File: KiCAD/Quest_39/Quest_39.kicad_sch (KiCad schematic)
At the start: 15 parts

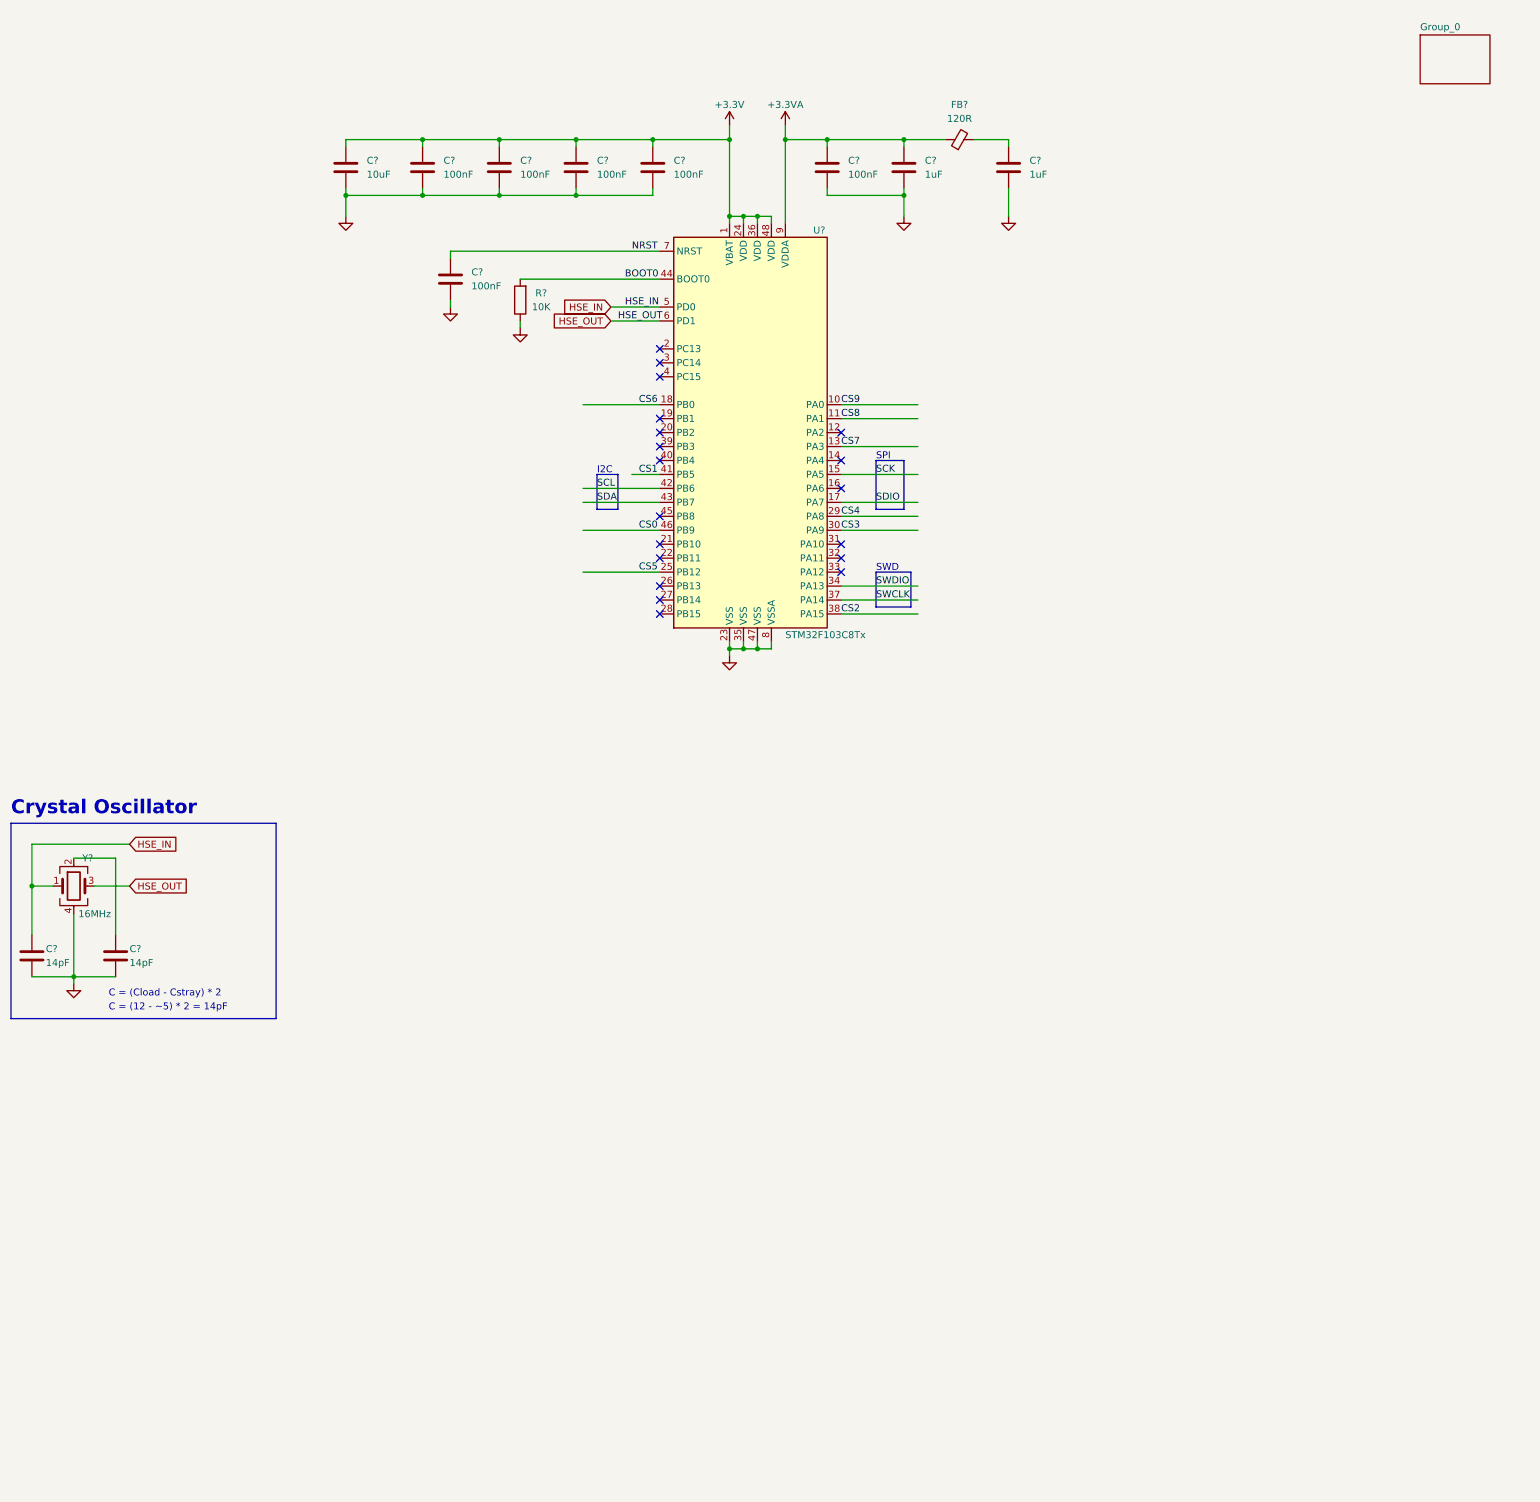
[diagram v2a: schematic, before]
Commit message: Ordered BUCK_x schematic pages
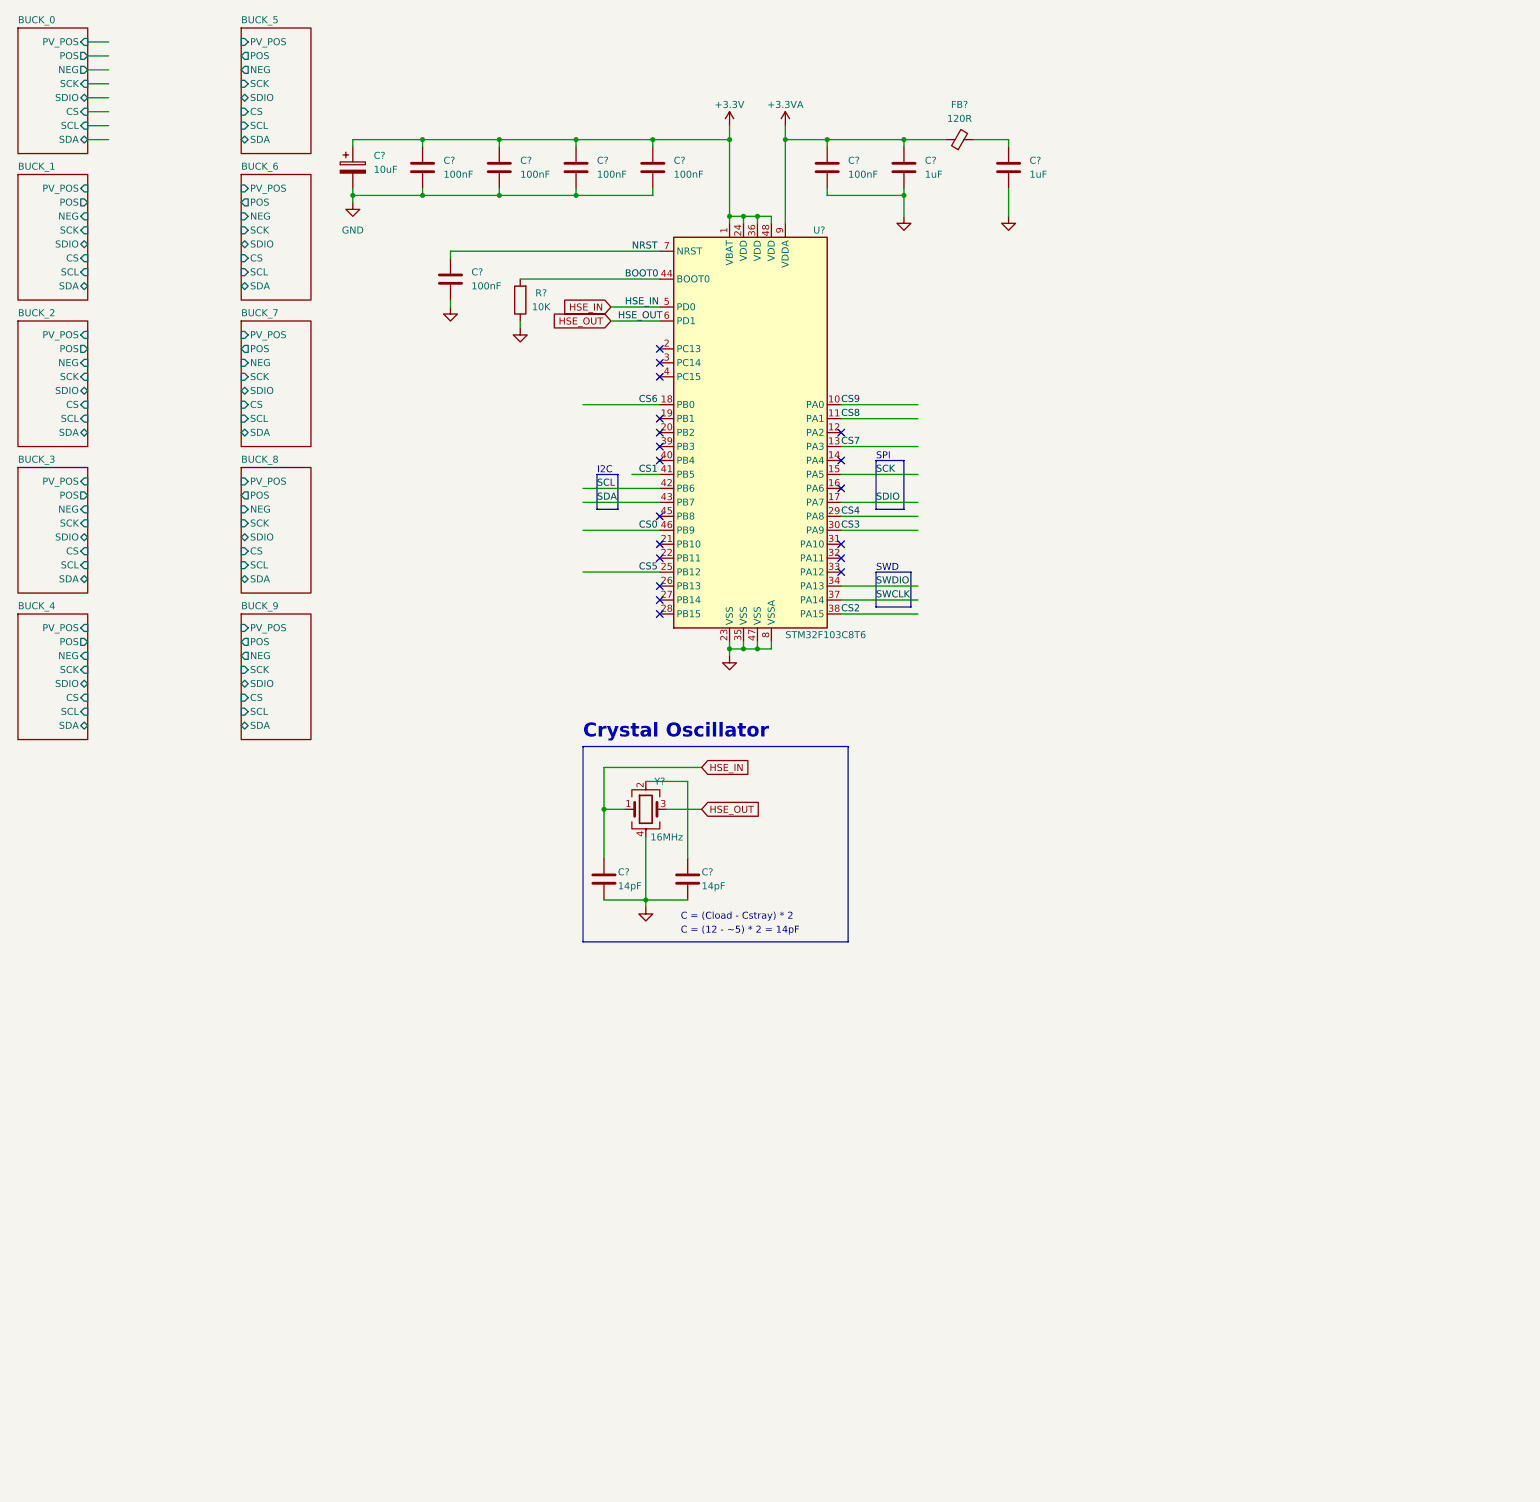
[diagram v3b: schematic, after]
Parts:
- removed C?: 10uF, symbol Device:C
- added C?: 10uF, symbol Device:C_Polarized
- U?: value STM32F103C8Tx -> STM32F103C8T6
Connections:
- net +3.3V: now also C?.1
- net GND: now also C?.2
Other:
- sheet Group_0 renamed BUCK_0
- added sheet BUCK_1 (BUCK_1.kicad_sch)
- added sheet BUCK_2 (BUCK_2.kicad_sch)
- added sheet BUCK_3 (BUCK_3.kicad_sch)
- added sheet BUCK_4 (BUCK_4.kicad_sch)
- added sheet BUCK_5 (BUCK_5.kicad_sch)
- added sheet BUCK_6 (BUCK_6.kicad_sch)
- added sheet BUCK_7 (BUCK_7.kicad_sch)
- added sheet BUCK_8 (BUCK_8.kicad_sch)
- added sheet BUCK_9 (BUCK_9.kicad_sch)
- sheet BUCK_0: file Quest_39_blz2.kicad_sch -> BUCK_0.kicad_sch
- sheet BUCK_0 ports: added CS, NEG, POS, PV_POS, SCK, SCL, SDA, SDIO; removed none
- moved on the sheet: C?, Y?

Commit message: Added screw terminals. Ordered nets and added seperation between systems.
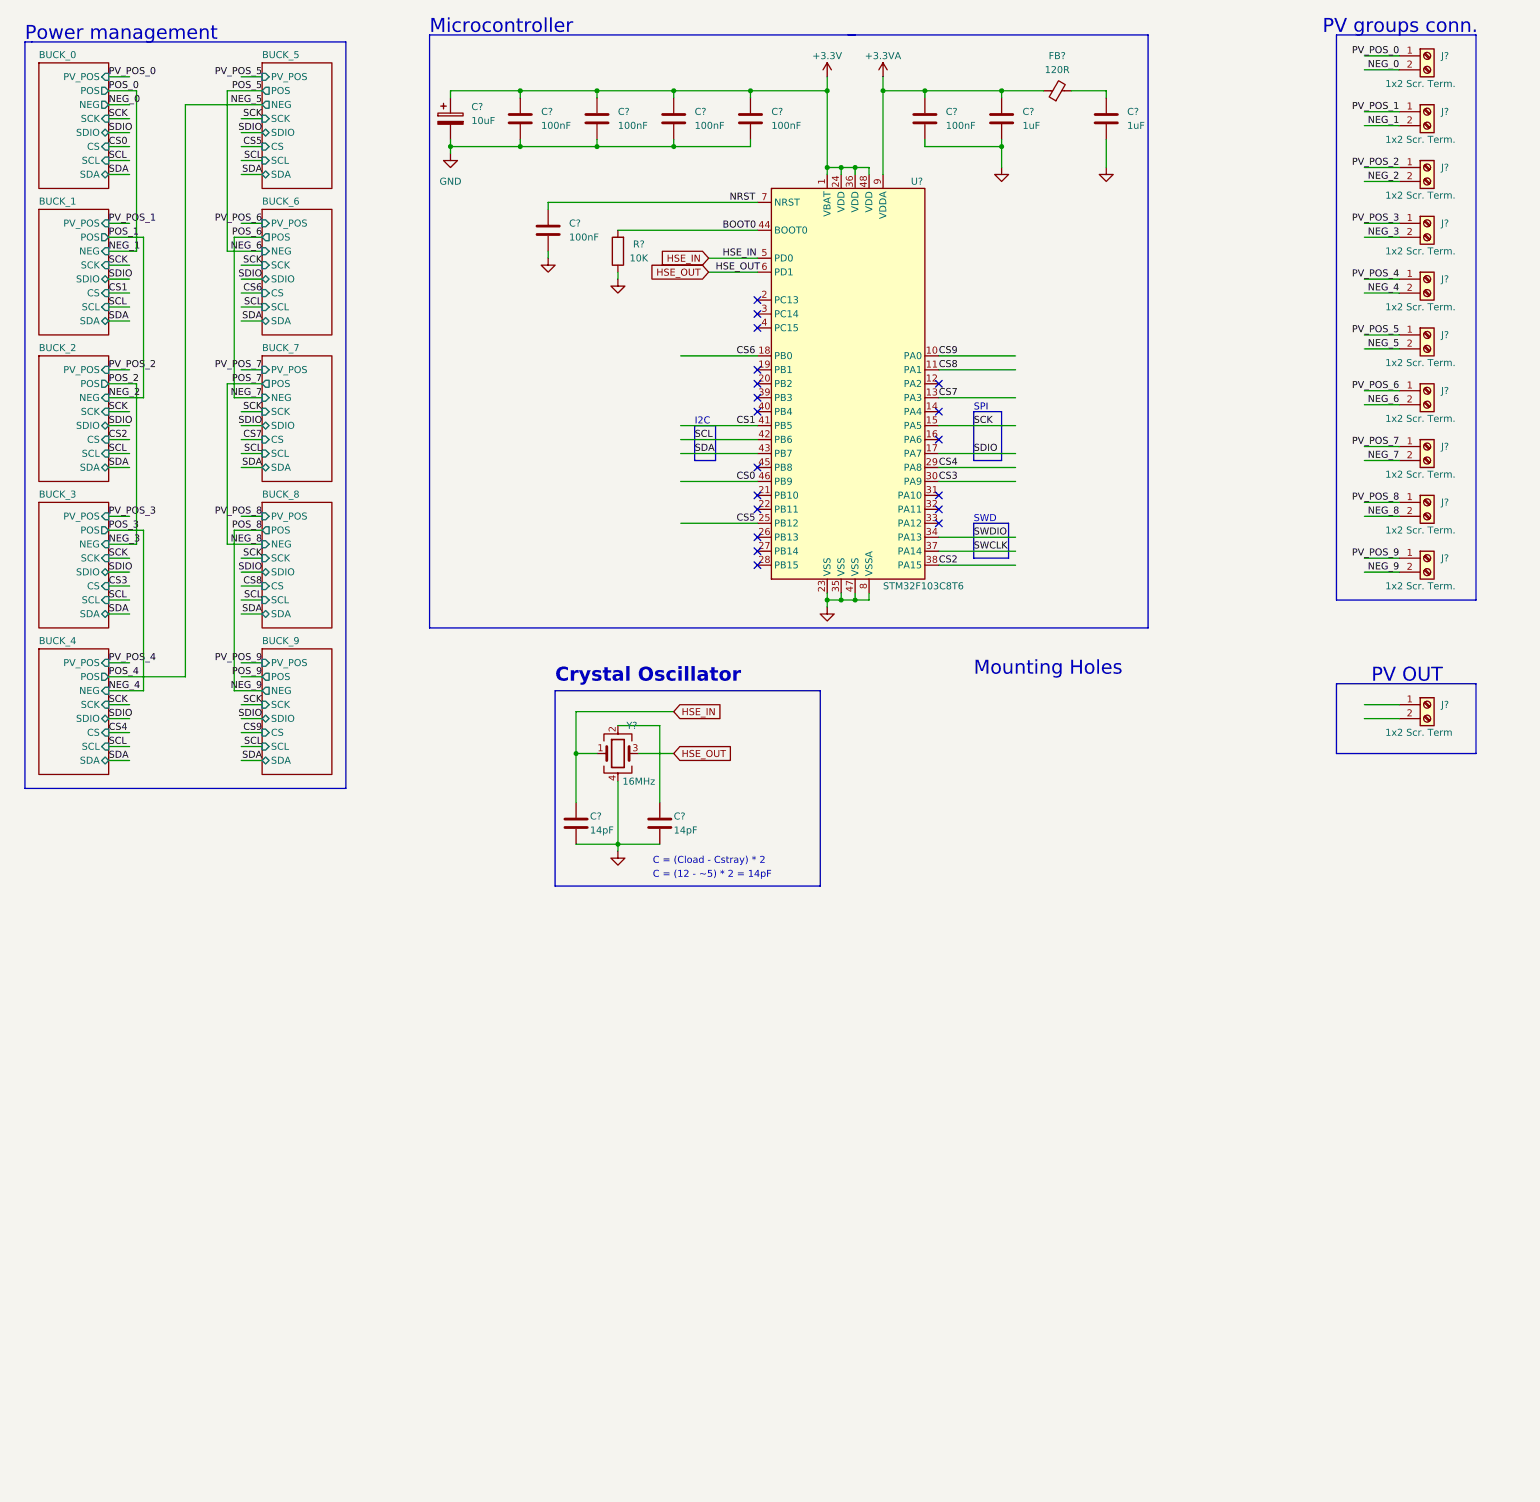
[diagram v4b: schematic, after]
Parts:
- added J? (x10): 1x2 Scr. Term., symbol Connector:Screw_Terminal_01x02
- added J?: 1x2 Scr. Term, symbol Connector:Screw_Terminal_01x02
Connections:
- new net NEG_0: J?.2 (Pin_2)
- new net NEG_1: J?.2 (Pin_2)
- new net NEG_2: J?.2 (Pin_2)
- new net NEG_3: J?.2 (Pin_2)
- new net NEG_4: J?.2 (Pin_2)
- new net NEG_5: J?.2 (Pin_2)
- new net NEG_6: J?.2 (Pin_2)
- new net NEG_7: J?.2 (Pin_2)
- new net NEG_8: J?.2 (Pin_2)
- new net NEG_9: J?.2 (Pin_2)
- new net PV_POS_0: J?.1 (Pin_1)
- new net PV_POS_1: J?.1 (Pin_1)
- new net PV_POS_2: J?.1 (Pin_1)
- new net PV_POS_3: J?.1 (Pin_1)
- new net PV_POS_4: J?.1 (Pin_1)
- new net PV_POS_5: J?.1 (Pin_1)
- new net PV_POS_6: J?.1 (Pin_1)
- new net PV_POS_7: J?.1 (Pin_1)
- new net PV_POS_8: J?.1 (Pin_1)
- new net PV_POS_9: J?.1 (Pin_1)
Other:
- note added: "Microcontroller"
- note added: "Mounting Holes"
- note added: "PV OUT"
- note added: "PV groups conn."
- note added: "Power management"
- moved on the sheet: C?, FB?, R?, U?, Y?

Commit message: Changed root schematic to A3 size.
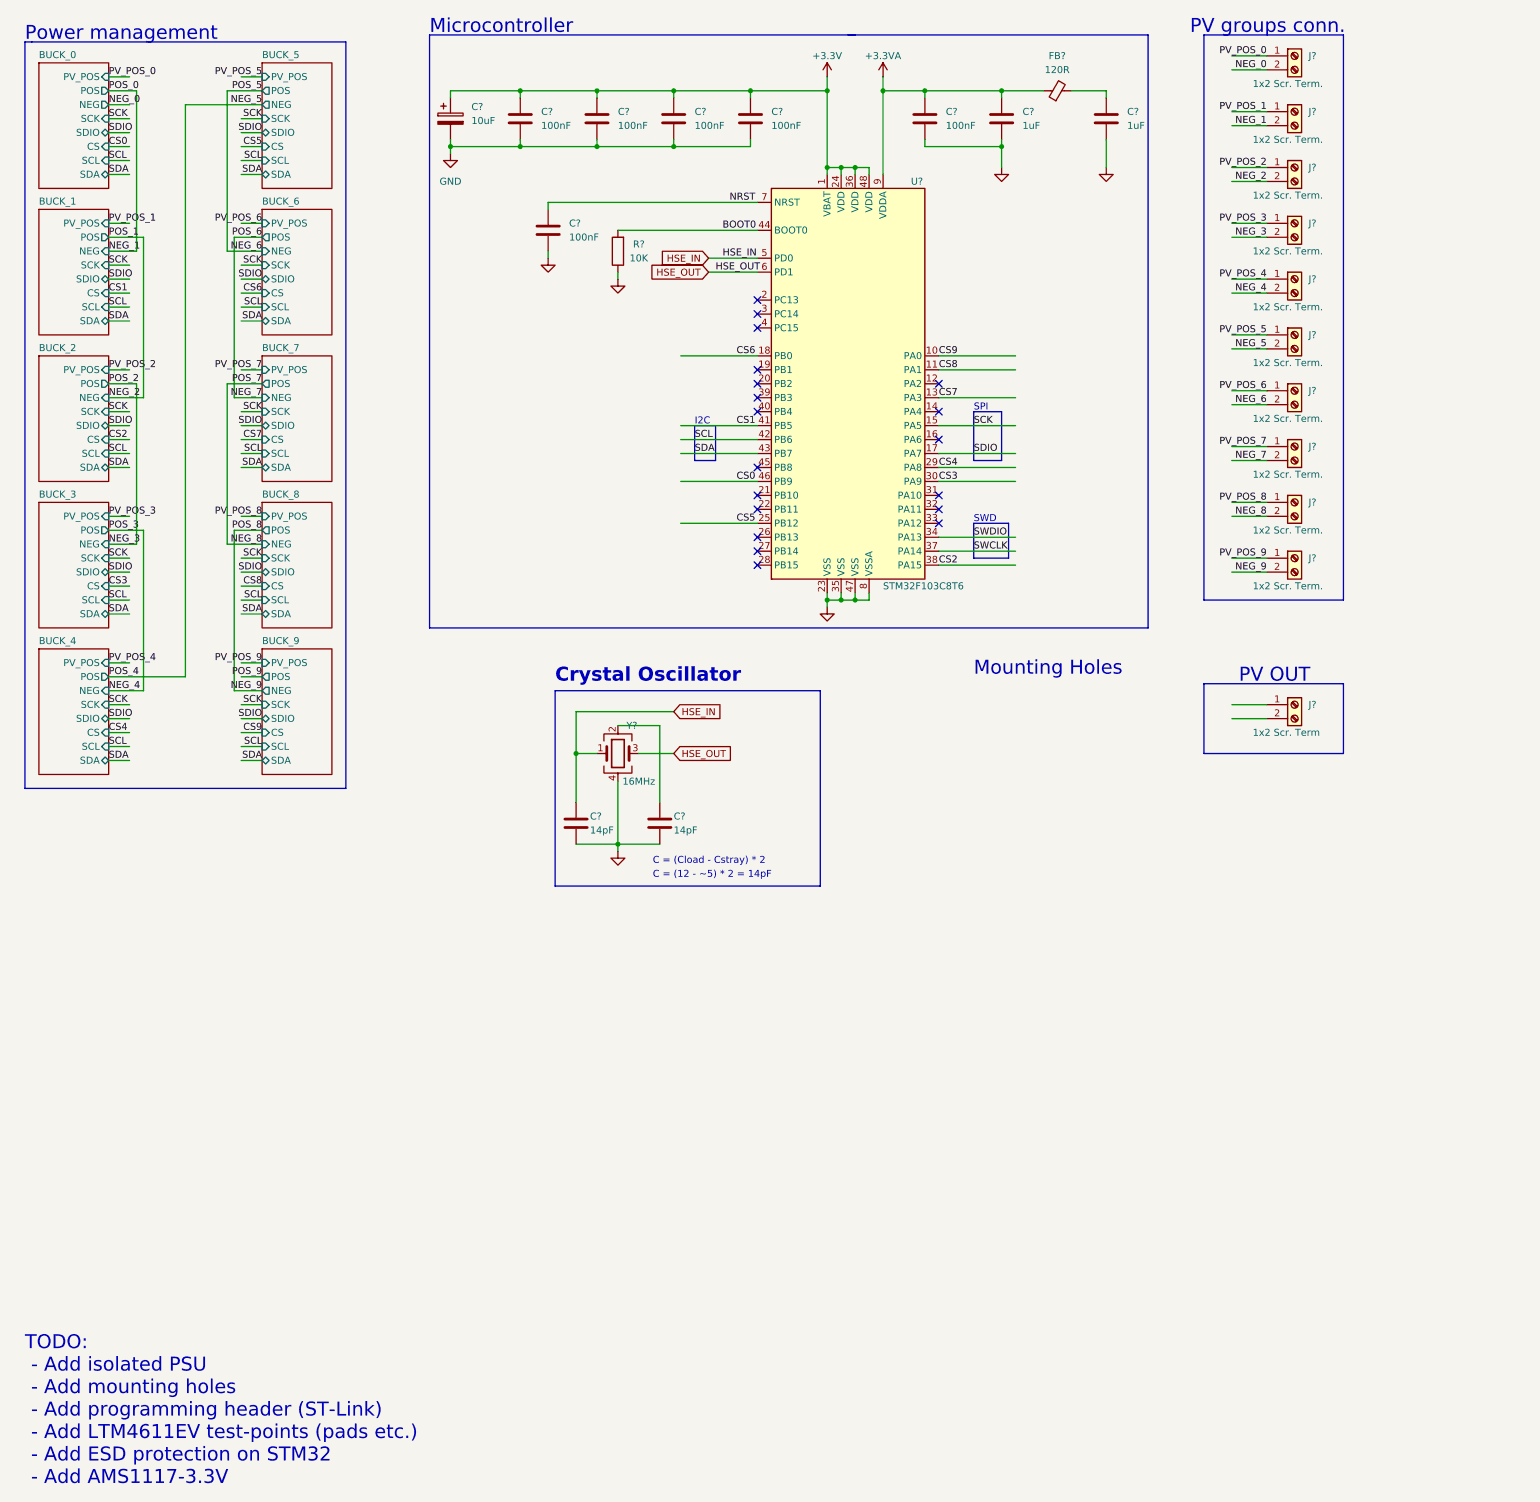
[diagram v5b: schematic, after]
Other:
- note added: "TODO: - Add isolated PSU - Add mounting holes - Add programming header (ST-Link) - Add LTM4611EV test-points (pads etc.) - Add ESD protection on STM32 - Add AMS1117-3.3V"
- moved on the sheet: J?
